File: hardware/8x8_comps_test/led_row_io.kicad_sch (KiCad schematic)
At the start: 3 parts

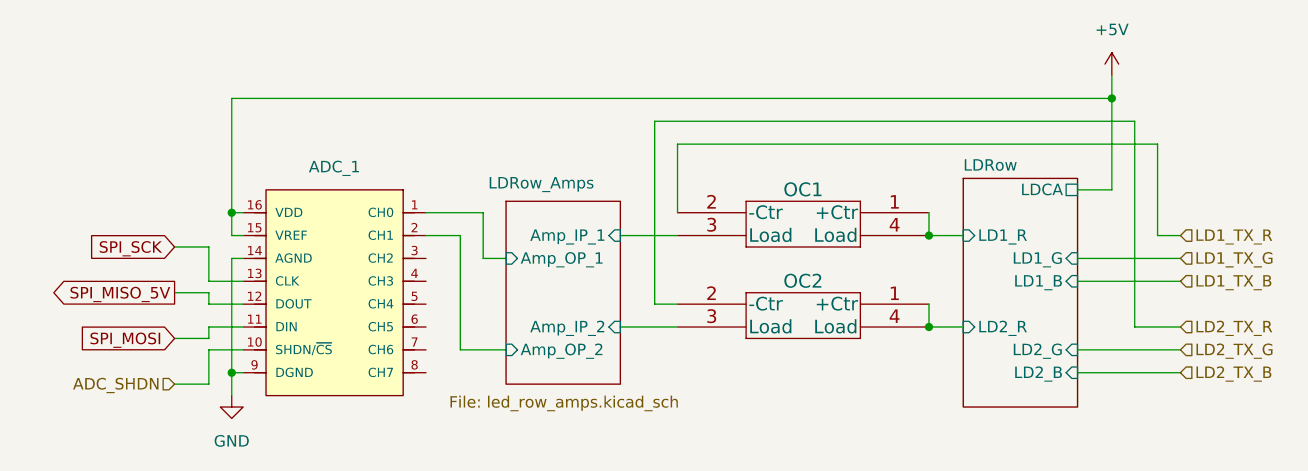
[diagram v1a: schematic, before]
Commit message: Updated Footprints
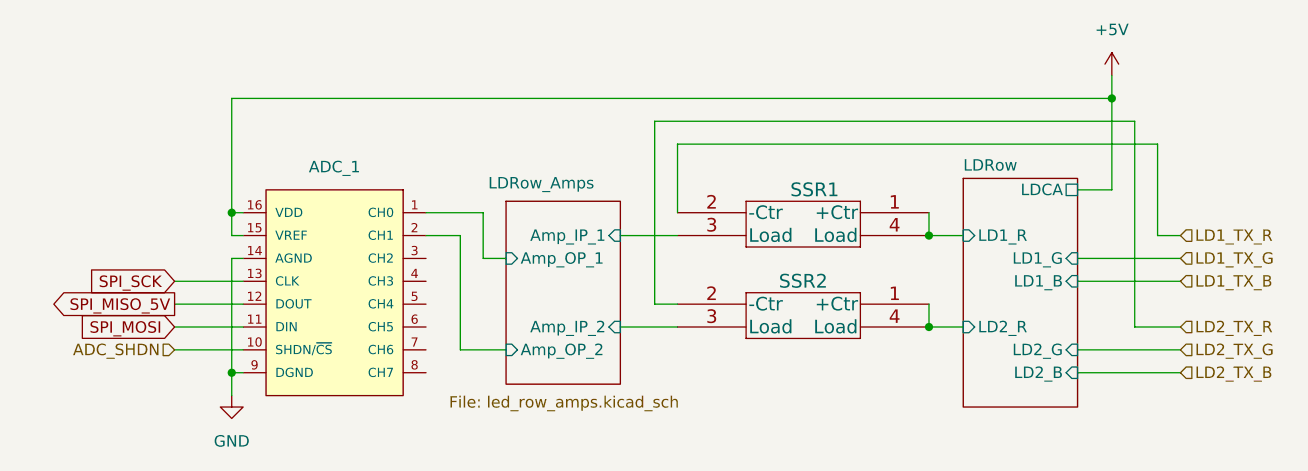
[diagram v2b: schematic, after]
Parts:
- ADC_1: footprint ADC:MCP3008-I&slash_P -> (none)
- SSR1: renamed from OC1; value CPC1125N -> TLP417A-TP-F; footprint Opto-coupler:footprints -> SSR:footprints; symbol Opto-coupler:CPC1125N -> SSR:TLP4176ATP_F
- SSR2: renamed from OC2; value CPC1125N -> TLP417A-TP-F; footprint Opto-coupler:footprints -> SSR:footprints; symbol Opto-coupler:CPC1125N -> SSR:TLP4176ATP_F
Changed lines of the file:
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@@
   (junction (at 34.29 95.25) (diameter 0) (color 0 0 0 0)
   )
+  (junction (at 34.29 77.47) (diameter 0) (color 0 0 0 0)
+  )
   (junction (at 111.76 80.01) (diameter 0) (color 0 0 0 0)
   )
-  (junction (at 34.29 77.47) (diameter 0) (color 0 0 0 0)
-  )
   (junction (at 132.08 64.77) (diameter 0) (color 0 0 0 0)
   )
@@
     (stroke (width 0) (type default) (color 0 0 0 0))
   )
-  (wire (pts (xy 31.75 96.52) (xy 31.75 92.71))
-    (stroke (width 0) (type default) (color 0 0 0 0))
-  )
   (wire (pts (xy 34.29 77.47) (xy 34.29 80.01))
     (stroke (width 0) (type default) (color 0 0 0 0))
@@
     (stroke (width 0) (type default) (color 0 0 0 0))
   )
-  (wire (pts (xy 27.94 86.36) (xy 31.75 86.36))
-    (stroke (width 0) (type default) (color 0 0 0 0))
-  )
-  (wire (pts (xy 59.69 92.71) (xy 59.69 80.01))
-    (stroke (width 0) (type default) (color 0 0 0 0))
-  )
   (wire (pts (xy 64.77 82.55) (xy 62.23 82.55))
     (stroke (width 0) (type default) (color 0 0 0 0))
@@
     (stroke (width 0) (type default) (color 0 0 0 0))
   )
+  (wire (pts (xy 59.69 80.01) (xy 59.69 92.71))
+    (stroke (width 0) (type default) (color 0 0 0 0))
+  )
   (wire (pts (xy 62.23 77.47) (xy 55.88 77.47))
     (stroke (width 0) (type default) (color 0 0 0 0))
   )
-  (wire (pts (xy 31.75 91.44) (xy 31.75 90.17))
-    (stroke (width 0) (type default) (color 0 0 0 0))
-  )
-  (wire (pts (xy 31.75 92.71) (xy 35.56 92.71))
+  (wire (pts (xy 27.94 92.71) (xy 35.56 92.71))
     (stroke (width 0) (type default) (color 0 0 0 0))
   )
@@
     (stroke (width 0) (type default) (color 0 0 0 0))
   )
-  (wire (pts (xy 27.94 81.28) (xy 31.75 81.28))
-    (stroke (width 0) (type default) (color 0 0 0 0))
-  )
   (wire (pts (xy 34.29 64.77) (xy 34.29 77.47))
     (stroke (width 0) (type default) (color 0 0 0 0))
@@
     (stroke (width 0) (type default) (color 0 0 0 0))
   )
-  (wire (pts (xy 27.94 96.52) (xy 31.75 96.52))
-    (stroke (width 0) (type default) (color 0 0 0 0))
-  )
   (wire (pts (xy 35.56 77.47) (xy 34.29 77.47))
     (stroke (width 0) (type default) (color 0 0 0 0))
@@
     (stroke (width 0) (type default) (color 0 0 0 0))
   )
-  (wire (pts (xy 31.75 87.63) (xy 35.56 87.63))
+  (wire (pts (xy 27.94 87.63) (xy 35.56 87.63))
     (stroke (width 0) (type default) (color 0 0 0 0))
   )
@@
     (stroke (width 0) (type default) (color 0 0 0 0))
   )
-  (wire (pts (xy 31.75 81.28) (xy 31.75 85.09))
-    (stroke (width 0) (type default) (color 0 0 0 0))
-  )
   (wire (pts (xy 111.76 90.17) (xy 115.57 90.17))
     (stroke (width 0) (type default) (color 0 0 0 0))
@@
     (stroke (width 0) (type default) (color 0 0 0 0))
   )
-  (wire (pts (xy 31.75 85.09) (xy 35.56 85.09))
-    (stroke (width 0) (type default) (color 0 0 0 0))
-  )
-  (wire (pts (xy 31.75 86.36) (xy 31.75 87.63))
+  (wire (pts (xy 27.94 85.09) (xy 35.56 85.09))
     (stroke (width 0) (type default) (color 0 0 0 0))
   )
@@
     (stroke (width 0) (type default) (color 0 0 0 0))
   )
-  (wire (pts (xy 27.94 91.44) (xy 31.75 91.44))
-    (stroke (width 0) (type default) (color 0 0 0 0))
-  )
-  (wire (pts (xy 31.75 90.17) (xy 35.56 90.17))
+  (wire (pts (xy 27.94 90.17) (xy 35.56 90.17))
     (stroke (width 0) (type default) (color 0 0 0 0))
   )
@@
     (stroke (width 0) (type default) (color 0 0 0 0))
   )
-  (global_label "SPI_MOSI" (shape input) (at 27.94 91.44 180) (fields_autoplaced)
-    (effects (font (size 1.27 1.27)) (justify right))
-    (property "Intersheet References" "${INTERSHEET_REFS}" (id 0) (at 16.8788 91.3606 0)
+  (global_label "SPI_MOSI" (shape input) (at 27.94 90.17 180) (fields_autoplaced)
+    (effects (font (size 1.27 1.27)) (justify right))
+    (property "Intersheet References" "${INTERSHEET_REFS}" (id 0) (at 16.8788 90.0906 0)
       (effects (font (size 1.27 1.27)) (justify right) hide)
     )
   )
-  (global_label "SPI_MISO_5V" (shape output) (at 27.94 86.36 180) (fields_autoplaced)
-    (effects (font (size 1.27 1.27)) (justify right))
-    (property "Intersheet References" "${INTERSHEET_REFS}" (id 0) (at 13.6131 86.2806 0)
+  (global_label "SPI_MISO_5V" (shape output) (at 27.94 87.63 180) (fields_autoplaced)
+    (effects (font (size 1.27 1.27)) (justify right))
+    (property "Intersheet References" "${INTERSHEET_REFS}" (id 0) (at 13.6131 87.5506 0)
       (effects (font (size 1.27 1.27)) (justify right) hide)
     )
   )
-  (global_label "SPI_SCK" (shape input) (at 27.94 81.28 180) (fields_autoplaced)
-    (effects (font (size 1.27 1.27)) (justify right))
-    (property "Intersheet References" "${INTERSHEET_REFS}" (id 0) (at 17.7255 81.2006 0)
+  (global_label "SPI_SCK" (shape input) (at 27.94 85.09 180) (fields_autoplaced)
+    (effects (font (size 1.27 1.27)) (justify right))
+    (property "Intersheet References" "${INTERSHEET_REFS}" (id 0) (at 17.7255 85.0106 0)
       (effects (font (size 1.27 1.27)) (justify right) hide)
     )
   )
-  (hierarchical_label "ADC_SHDN" (shape input) (at 27.94 96.52 180)
+  (hierarchical_label "ADC_SHDN" (shape input) (at 27.94 92.71 180)
     (effects (font (size 1.27 1.27)) (justify right))
   )
@@
       (effects (font (size 1.27 1.27)) hide)
     )
-    (property "Footprint" "ADC:MCP3008-I&slash_P" (id 2) (at 58.42 100.33 0)
+    (property "Footprint" "" (id 2) (at 58.42 100.33 0)
       (effects (font (size 1.27 1.27)) (justify left bottom) hide)
     )
@@
     (pin "9")
   )
-  (symbol (lib_name "CPC1125N_1") (lib_id "Opto-coupler:CPC1125N") (at 111.76 87.63 0) (mirror y) (unit 1)
+  (symbol (lib_id "SSR:TLP4176ATP_F") (at 97.79 88.9 0) (mirror y) (unit 1)
     (in_bom yes) (on_board yes)
-    (property "Reference" "OC2" (id 0) (at 97.79 85.09 0)
-      (effects (font (size 1.524 1.524)))
-    )
-    (property "Value" "CPC1125N" (id 1) (at 104.14 92.71 0)
+    (property "Reference" "SSR2" (id 0) (at 97.79 85.09 0)
+      (effects (font (size 1.524 1.524)))
+    )
+    (property "Value" "TLP417A-TP-F" (id 1) (at 90.17 93.98 0)
       (effects (font (size 1.524 1.524)) (justify left) hide)
     )
-    (property "Footprint" "Opto-coupler:footprints" (id 2) (at 99.06 85.09 0)
+    (property "Footprint" "SSR:footprints" (id 2) (at 97.79 85.09 0)
       (effects (font (size 1.524 1.524)) hide)
     )
-    (property "Datasheet" "" (id 3) (at 111.76 87.63 0)
-      (effects (font (size 1.524 1.524)) hide)
+    (property "Datasheet" "" (id 3) (at 111.76 93.98 0)
+      (effects (font (size 1.524 1.524)))
     )
     (pin "1")
@@
     (pin "1")
   )
-  (symbol (lib_name "CPC1125N_1") (lib_id "Opto-coupler:CPC1125N") (at 111.76 77.47 0) (mirror y) (unit 1)
+  (symbol (lib_id "SSR:TLP4176ATP_F") (at 97.79 78.74 0) (mirror y) (unit 1)
     (in_bom yes) (on_board yes)
-    (property "Reference" "OC1" (id 0) (at 97.79 74.93 0)
-      (effects (font (size 1.524 1.524)))
-    )
-    (property "Value" "CPC1125N" (id 1) (at 104.14 82.55 0)
+    (property "Reference" "SSR1" (id 0) (at 99.06 74.93 0)
+      (effects (font (size 1.524 1.524)))
+    )
+    (property "Value" "TLP417A-TP-F" (id 1) (at 90.17 83.82 0)
       (effects (font (size 1.524 1.524)) (justify left) hide)
     )
-    (property "Footprint" "Opto-coupler:footprints" (id 2) (at 99.06 74.93 0)
+    (property "Footprint" "SSR:footprints" (id 2) (at 97.79 74.93 0)
       (effects (font (size 1.524 1.524)) hide)
     )
-    (property "Datasheet" "" (id 3) (at 111.76 77.47 0)
-      (effects (font (size 1.524 1.524)) hide)
-    )
-    (pin "1")
+    (property "Datasheet" "" (id 3) (at 111.76 83.82 0)
+      (effects (font (size 1.524 1.524)))
+    )
+    (pin "1")

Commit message: Updated Placement
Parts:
- ADC_1: footprint (none) -> ADC:MCP3008-I&slash_P
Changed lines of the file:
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@@
       (effects (font (size 1.27 1.27)) hide)
     )
-    (property "Footprint" "" (id 2) (at 58.42 100.33 0)
+    (property "Footprint" "ADC:MCP3008-I&slash_P" (id 2) (at 58.42 100.33 0)
       (effects (font (size 1.27 1.27)) (justify left bottom) hide)
     )

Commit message: Updated PCB
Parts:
- removed ADC_1: MCU-MCP3008-I/P(DIP16-7.62MM), ADC:MCP3008-I&slash_P, symbol ADC:MCU-MCP3008-I{brace}slash}P(DIP16-7.62MM)
- removed SSR1, SSR2: TLP417A-TP-F, SSR:footprints, symbol SSR:TLP4176ATP_F
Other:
- removed sheet  LDRow_Amps
- removed sheet LDRow
